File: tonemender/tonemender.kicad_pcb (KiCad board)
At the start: 2 copper layers, 90.8 x 45.1 mm, 30 parts, among them J1 JACK_STEREO, J2 JACK_STEREO, P1 CONN_01X03, P2 CONN_01X01, U1 TL072

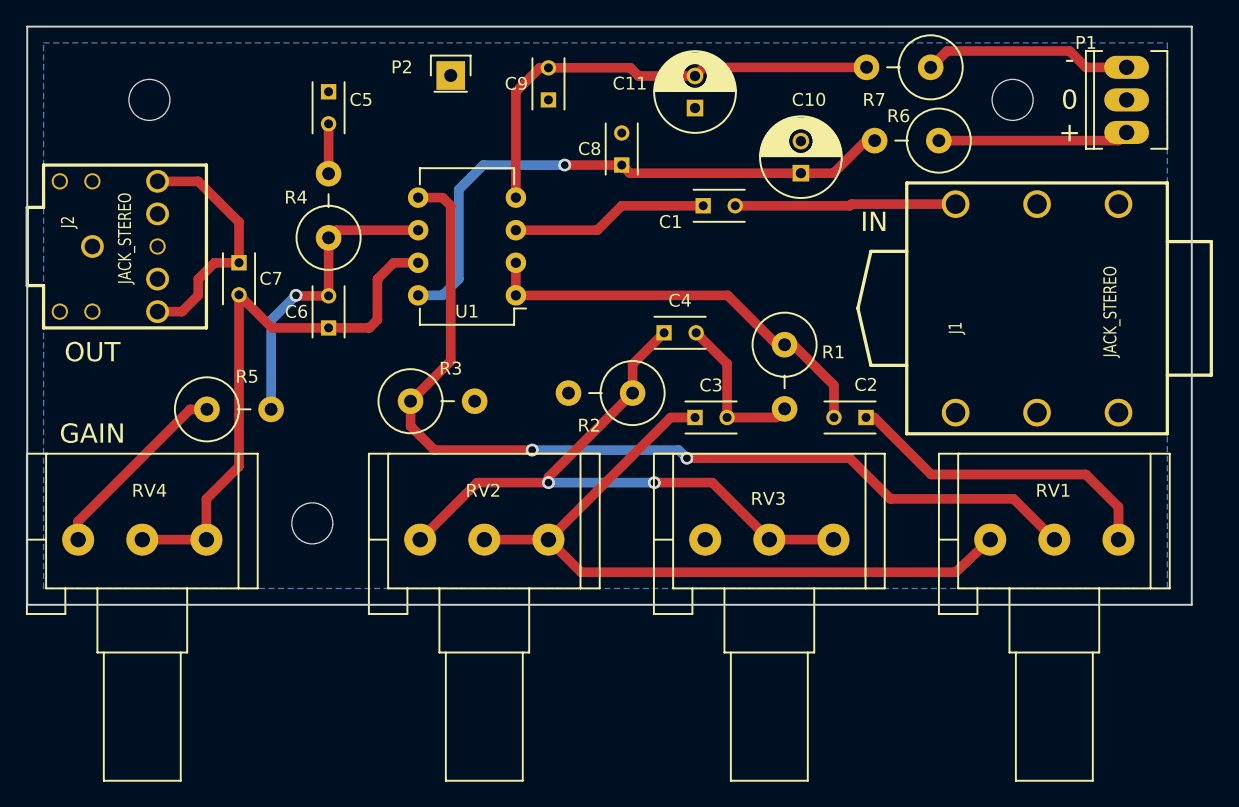
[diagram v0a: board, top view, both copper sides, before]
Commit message: Tonemender for Bass: 1. Updated the capacitor values 2. Shrank the PCB
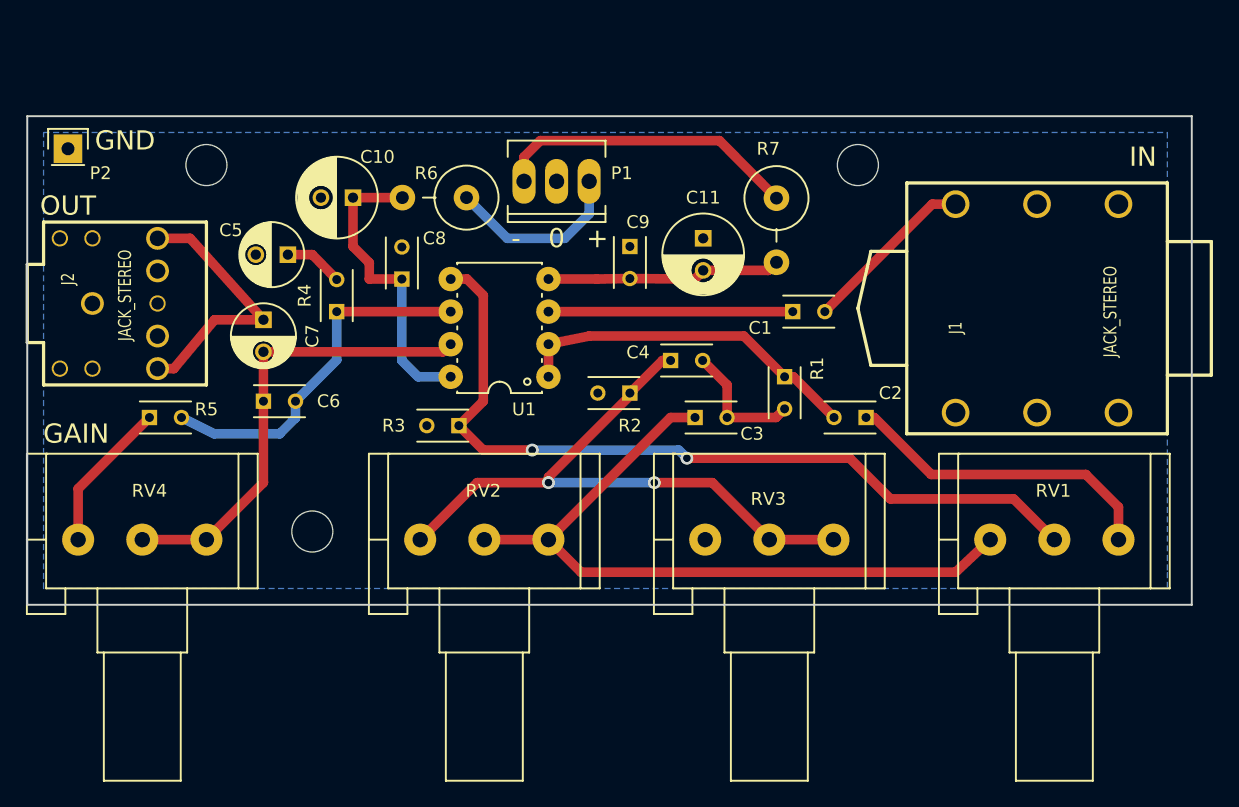
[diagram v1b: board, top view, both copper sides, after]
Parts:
- removed the REF** at (194.9, 93.3)
- removed the REF** at (127.6, 93.3)
- removed the REF** at (140.3, 126.4)
- added REF**: MountingHole_3.2mm_M3, Mounting_Holes:MountingHole_3.2mm_M3, F.Cu at (182.9, 98.4)
- added REF**: MountingHole_3.2mm_M3, Mounting_Holes:MountingHole_3.2mm_M3, F.Cu at (132.1, 98.4)
- added REF**: MountingHole_3.2mm_M3, Mounting_Holes:MountingHole_3.2mm_M3, F.Cu at (140.3, 127.0)
- C1: value 22nF -> 470nF
- C5: value 470nF -> 47uF; footprint Capacitors_ThroughHole:C_Rect_L4_W2.5_P2.5 -> Capacitors_ThroughHole:C_Radial_D5_L6_P2.5
- C6: value 47pF -> 47pF (optional)
- C7: value 470nF -> 1uF; footprint Capacitors_ThroughHole:C_Rect_L4_W2.5_P2.5 -> Capacitors_ThroughHole:C_Radial_D5_L6_P2.5
- R1, R2, R3, R4, R5: footprint Resistors_ThroughHole:Resistor_Vertical_RM5mm -> Capacitors_ThroughHole:C_Rect_L4_W2.5_P2.5
- U1: value TL072 -> OPA1612; footprint Housings_DIP:DIP-8_W7.62mm -> Power_Integrations:PDIP-8
- moved P1 44.9 mm to (159.4, 99.7), turned to 180 degrees
- moved R6 37.1 mm to (149.9, 101.0)
- moved C10 35.0 mm to (143.5, 101.0), turned to 180 degrees
- moved P2 30.4 mm to (121.3, 97.2)
- moved C8 19.3 mm to (147.3, 107.3)
- moved R7 15.9 mm to (176.5, 103.5), turned to 270 degrees
- moved C5 13.1 mm to (138.4, 105.4), turned to 180 degrees
- moved C9 13.1 mm to (165.1, 104.8), turned to 270 degrees
- moved C1 10.8 mm to (177.8, 109.9)
- moved C11 10.2 mm to (170.8, 104.1), turned to 270 degrees
- moved R4 8.28 mm to (142.2, 109.9)
- moved C6 7.65 mm to (136.5, 116.8), turned to 0 degrees
- moved R5 7.01 mm to (127.6, 118.1)
- moved C7 4.84 mm to (136.5, 110.5)
- moved J2 4.45 mm to (116.8, 102.9)
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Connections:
- C5 pad 1: GND -> Net-(C5-Pad1)
- C5 pad 2: Net-(C5-Pad2) -> GND
- R4 pad 2: Net-(C5-Pad2) -> Net-(C5-Pad1)
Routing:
- net +12V: track 45.2 -> 24.0 mm, vias 1 -> 0
- net -12V: track 36.9 -> 18.3 mm
- net Net-(R3-Pad1): track 75.2 -> 64.1 mm
- net Net-(C6-Pad1): track 44.1 -> 36.3 mm
- net Net-(P1-Pad3): track 16.3 -> 24.0 mm
- net Net-(C2-Pad2): track 32.8 -> 27.5 mm
- net Net-(C5-Pad1): track 0.00 -> 4.63 mm
- net Net-(C6-Pad2): track 24.0 -> 28.2 mm, vias 1 -> 0
- net Net-(C5-Pad2): track 3.89 -> 0.00 mm
- net Net-(C1-Pad1): track 15.4 -> 19.1 mm
- net Net-(C1-Pad2): track 17.2 -> 13.7 mm
- net Net-(R5-Pad1): track 15.1 -> 11.8 mm
- net Net-(C3-Pad2): track 12.4 -> 10.00 mm
- net Net-(C7-Pad1): track 19.5 -> 21.1 mm
- net Net-(C4-Pad1): track 51.3 -> 49.8 mm
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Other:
- board size 90.8 x 45.1 mm -> 90.8 x 38.1 mm
- board text added: "GND"
